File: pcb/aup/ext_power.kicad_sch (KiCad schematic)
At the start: 12 parts, among them J1 USB_C_Receptacle_USB2.0_16P, J2 Barral_Jack_12V, Q1 AO3401A, Q2 AO3401A, U2 USBLC6-2SC6

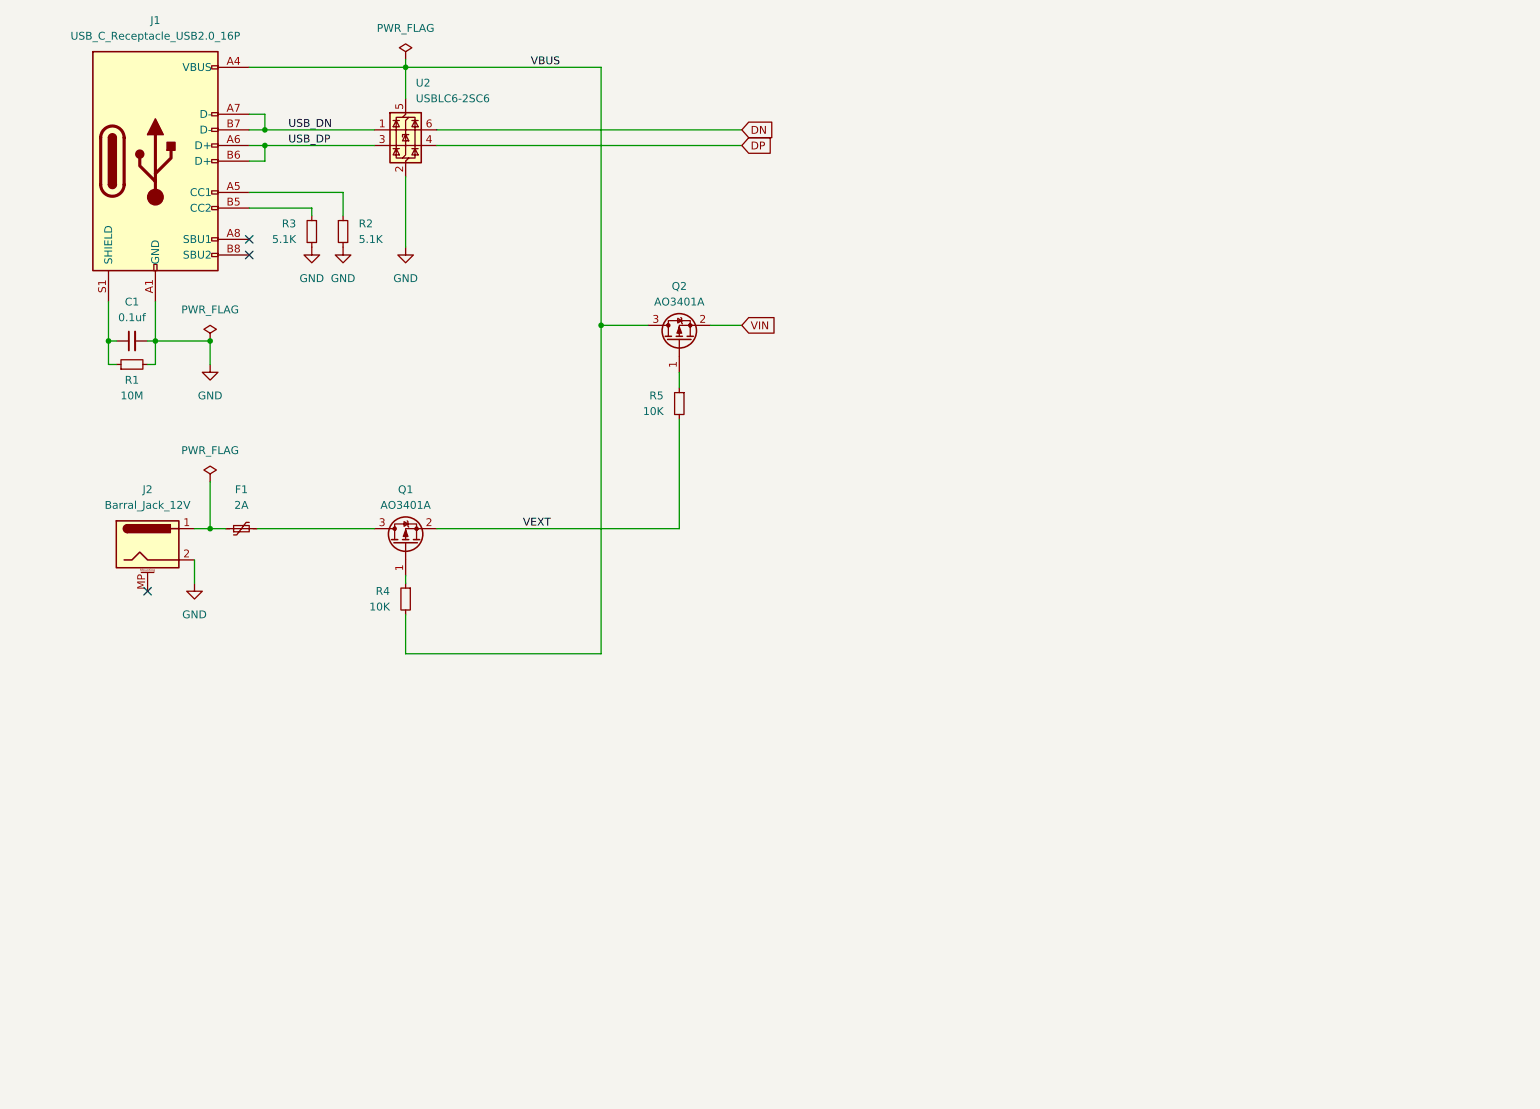
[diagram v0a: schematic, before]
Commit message: Add 5v regulator to external power portion
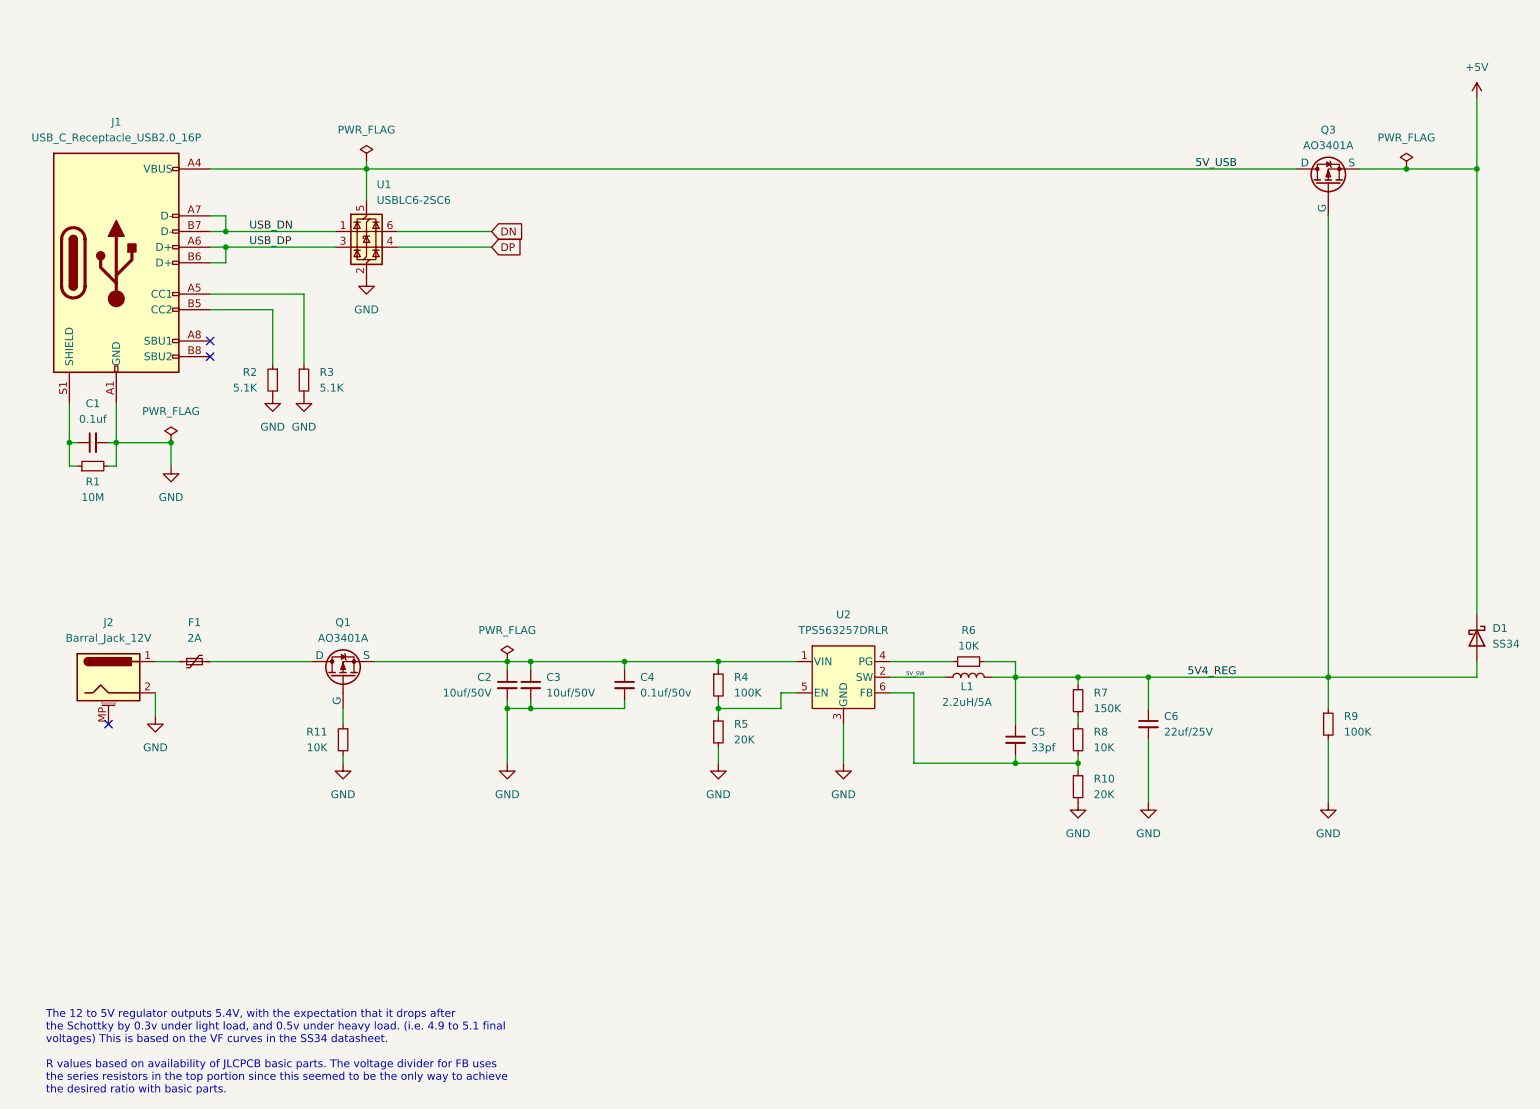
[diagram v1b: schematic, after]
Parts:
- removed R4, R5: 10K, Resistor_SMD:R_0603_1608Metric, symbol !Misc:R_10K_0603
- added C2, C3: 10uf/50V, Capacitor_SMD:C_0805_2012Metric, symbol !Misc:C_10uf_0805
- added C4: 0.1uf/50v, Capacitor_SMD:C_0603_1608Metric, symbol !Misc:C_0.1uf_0603
- added C5: 33pf, Capacitor_SMD:C_0402_1005Metric, symbol !Misc:C_33pf_0402
- added C6: 22uf/25V, Capacitor_SMD:C_0805_2012Metric, symbol !Misc:C_22uf_0805
- added D1: SS34, Diode_SMD:D_SMA, symbol !Misc:SS34
- added L1: 2.2uH/5A, Inductor_SMD:L_Sunlord_MWSA0518S, symbol !Misc:L_2.2uh_5A
- added R10, R5: 20K, Resistor_SMD:R_0603_1608Metric, symbol !Misc:R_20K_0603
- added R11, R6, R8: 10K, Resistor_SMD:R_0603_1608Metric, symbol !Misc:R_10K_0603
- added R4, R9: 100K, Resistor_SMD:R_0603_1608Metric, symbol !Misc:R_100K_0603
- added R7: 150K, Resistor_SMD:R_0603_1608Metric, symbol !Misc:R_150K_0603
- added U2: TPS563257DRLR, Package_TO_SOT_SMD:SOT-563, symbol !Misc:TPS563257DRLR
- renumbered Q2 to Q3, R3 to R2, R2 to R3, U2 to U1
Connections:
- net GND: now also C2.2, C3.2, C4.2, C6.2, R10.2, R11.2, R5.2, R9.2, U2.3 (GND)
- net at Q1.1 (G): now also R11.1
- net 5V4_REG: now reaches Q3.1 (G)
- net 5V4_REG: now also C5.1, C6.1, D1.2 (A), L1.2, R6.2, R7.1, R9.1
- net VBUS renamed 5V_USB
- net VEXT: no longer names the net of Q1.2 (S)
- net VEXT: now also C2.1, C3.1, C4.1, R4.1, U2.1 (VIN)
- net VIN renamed +5V
- net +5V: now also D1.1 (K)
- new net: R7.2, R8.1
- new net: R6.1, U2.4 (PG)
- new net: R4.2, R5.1, U2.5 (EN)
- new net: C5.2, R10.1, R8.2, U2.6 (FB)
- new net 5V_SW: L1.1, U2.2 (SW)
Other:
- note added: "The 12 to 5V regulator outputs 5.4V, with the expectation that it drops after the Schottky by 0.3v under light load, and 0.5v under heavy load. (i.e. 4.9 to 5.1 final voltages) This is based on the VF curves in the SS34 datasheet. R values based on availability of JLCPCB basic parts. The voltage divider for FB uses the series resistors in the top portion since this seemed to be the only way to ac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"
- moved on the sheet: C1, F1, J1, J2, Q3, R1, R2, R3, U1

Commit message: Start of fpga voltage rails. Added 1v0/vccint
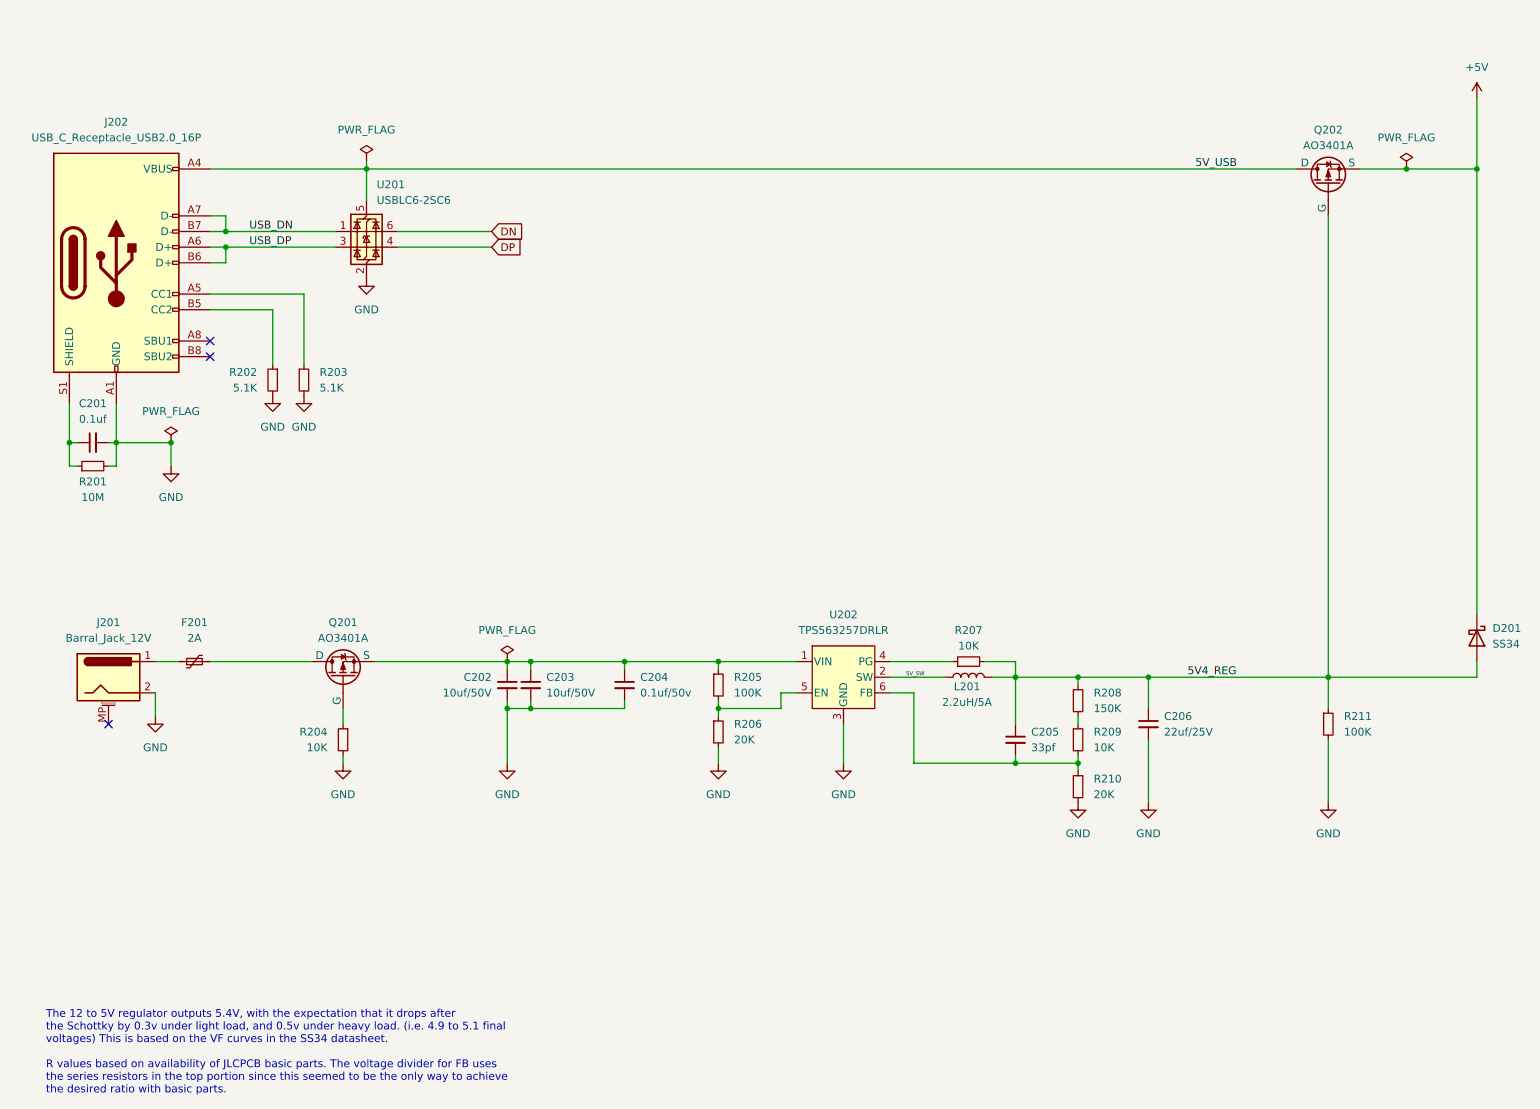
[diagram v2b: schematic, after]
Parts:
- renumbered C1 to C201, C2 to C202, C3 to C203, C4 to C204, C5 to C205, C6 to C206, D1 to D201, F1 to F201, J2 to J201, J1 to J202, L1 to L201, Q1 to Q201, Q3 to Q202, R1 to R201, R2 to R202, R3 to R203, R11 to R204, R4 to R205, R5 to R206, R6 to R207, R7 to R208, R8 to R209, R10 to R210, R9 to R211, U1 to U201, U2 to U202

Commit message: Finished voltage rail schematic
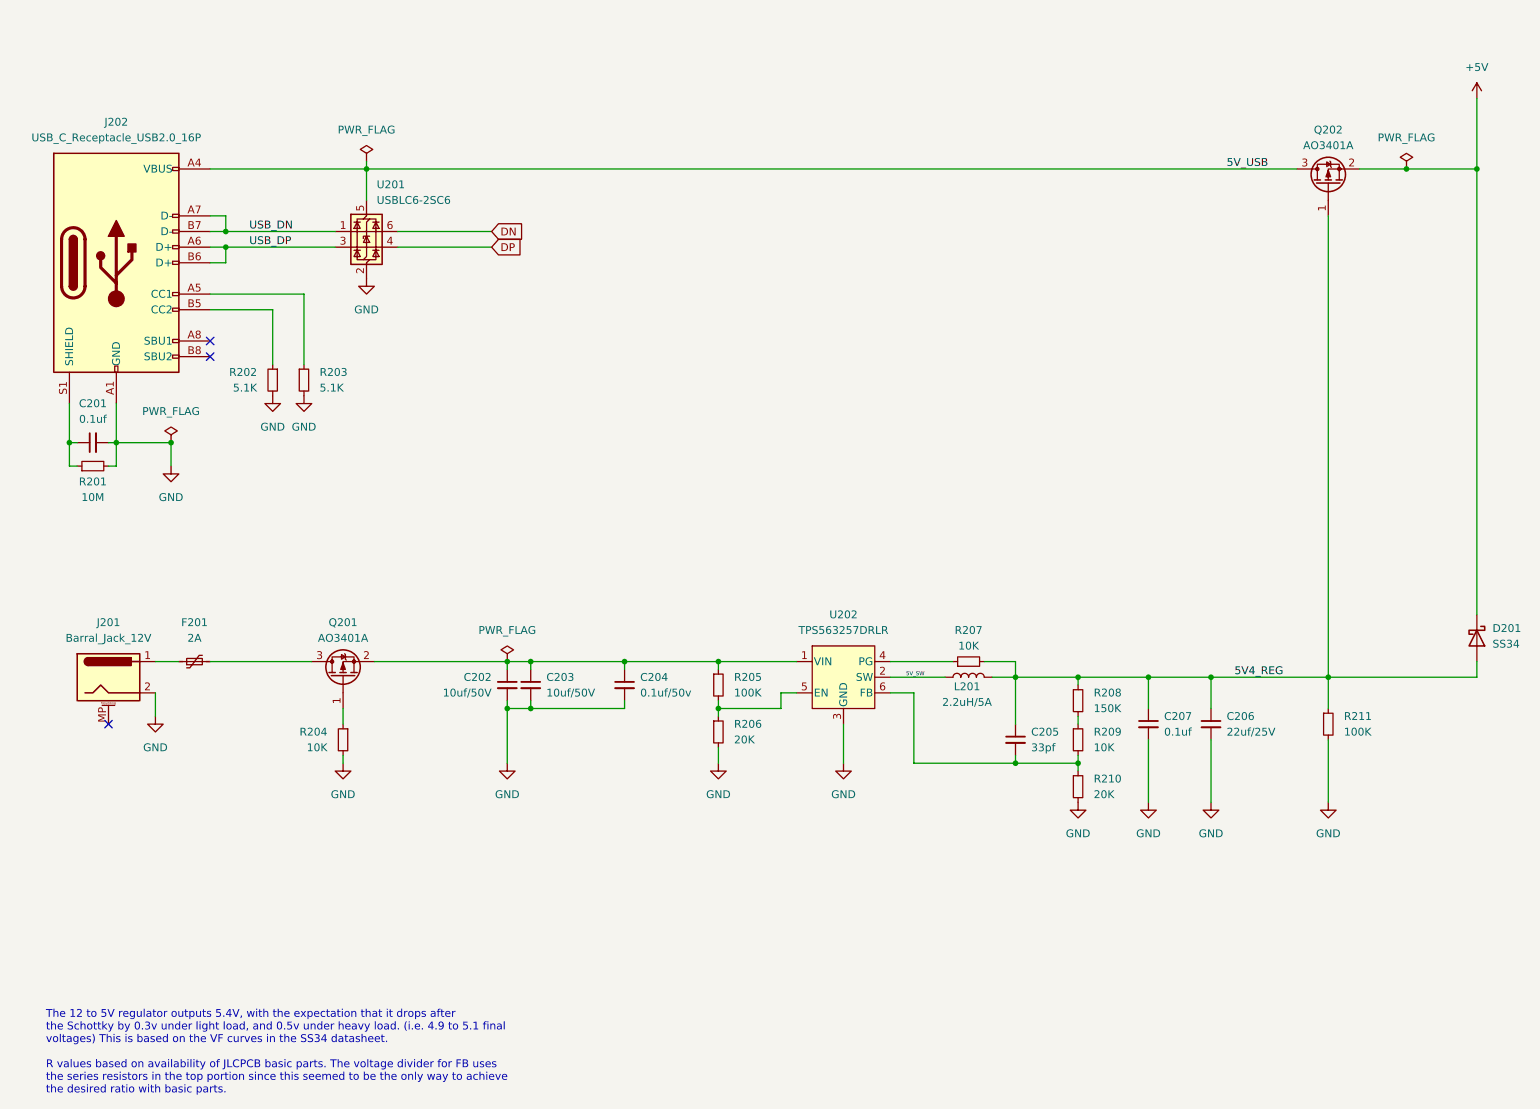
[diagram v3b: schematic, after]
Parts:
- added C207: 0.1uf, Capacitor_SMD:C_0402_1005Metric, symbol !Misc:C_0.1uf_0402
- U202: footprint Package_TO_SOT_SMD:SOT-563 -> SOT6_DRL_TEX
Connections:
- net 5V4_REG: now also C207.1
- net GND: now also C207.2
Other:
- moved on the sheet: C206
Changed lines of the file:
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@@
 	)
 	(junction
+		(at 209.55 128.27)
+		(diameter 0)
+		(color 0 0 0 0)
+	)
+	(junction
 		(at 72.39 45.72)
 		(diameter 0)
@@
 	(wire
 		(pts
+			(xy 209.55 138.43) (xy 209.55 148.59)
+		)
+		(stroke
+			(width 0)
+			(type default)
+		)
+	)
+	(wire
+		(pts
 			(xy 38.1 130.81) (xy 38.1 134.62)
 		)
@@
 	(wire
 		(pts
+			(xy 209.55 128.27) (xy 228.6 128.27)
+		)
+		(stroke
+			(width 0)
+			(type default)
+		)
+	)
+	(wire
+		(pts
 			(xy 252.73 125.73) (xy 252.73 128.27)
 		)
@@
 	(wire
 		(pts
+			(xy 209.55 128.27) (xy 209.55 133.35)
+		)
+		(stroke
+			(width 0)
+			(type default)
+		)
+	)
+	(wire
+		(pts
 			(xy 187.96 134.62) (xy 187.96 135.89)
 		)
@@
 	(wire
 		(pts
-			(xy 199.39 128.27) (xy 228.6 128.27)
+			(xy 199.39 128.27) (xy 209.55 128.27)
 		)
 		(stroke
@@
 	)
 	(label "5V_USB"
-		(at 207.01 45.72 0)
+		(at 212.09 45.72 0)
 		(effects
 			(font
@@
 	)
 	(label "5V4_REG"
-		(at 205.74 128.27 0)
+		(at 213.36 128.27 0)
 		(effects
 			(font
@@
 			)
 		)
-		(property "Footprint" "Package_TO_SOT_SMD:SOT-563"
+		(property "Footprint" "SOT6_DRL_TEX"
 			(at 136.906 116.586 0)
 			(effects
@@
 	)
 	(symbol
+		(lib_id "power:GND")
+		(at 209.55 148.59 0)
+		(unit 1)
+		(exclude_from_sim no)
+		(in_bom yes)
+		(on_board yes)
+		(dnp no)
+		(fields_autoplaced yes)
+		(property "Reference" "#PWR0216"
+			(at 209.55 154.94 0)
+			(effects
+				(font
+					(size 1.27 1.27)
+				)
+				(hide yes)
+			)
+		)
+		(property "Value" "GND"
+			(at 209.55 153.67 0)
+			(effects
+				(font
+					(size 1.27 1.27)
+				)
+			)
+		)
+		(property "Footprint" ""
+			(at 209.55 148.59 0)
+			(effects
+				(font
+					(size 1.27 1.27)
+				)
+				(hide yes)
+			)
+		)
+		(property "Datasheet" ""
+			(at 209.55 148.59 0)
+			(effects
+				(font
+					(size 1.27 1.27)
+				)
+				(hide yes)
+			)
+		)
+		(property "Description" "Power symbol creates a global label with name \"GND\" , ground"
+			(at 209.55 148.59 0)
+			(effects
+				(font
+					(size 1.27 1.27)
+				)
+				(hide yes)
+			)
+		)
+		(pin "1"
+		)
+		(instances
+			(project "aup"
+				(path "/312a869c-f247-4883-8e23-bdad51e1754f/66f6f111-4301-4b77-9bf5-52f6219d7e81"
+					(reference "#PWR0216")
+					(unit 1)
+				)
+			)
+		)
+	)
+	(symbol
 		(lib_id "!Misc:USBLC6-2SC6")
 		(at 72.39 55.88 0)
@@
 	)
 	(symbol
-		(lib_name "AO3401A_1")
 		(lib_id "!Misc:AO3401A")
 		(at 68.58 128.27 90)
@@
 	)
 	(symbol
+		(lib_id "!Misc:C_0.1uf_0402")
+		(at 199.39 135.89 0)
+		(unit 1)
+		(exclude_from_sim no)
+		(in_bom yes)
+		(on_board yes)
+		(dnp no)
+		(fields_autoplaced yes)
+		(property "Reference" "C207"
+			(at 201.93 134.6262 0)
+			(effects
+				(font
+					(size 1.27 1.27)
+				)
+				(justify left)
+			)
+		)
+		(property "Value" "0.1uf"
+			(at 201.93 137.1662 0)
+			(effects
+				(font
+					(size 1.27 1.27)
+				)
+				(justify left)
+			)
+		)
+		(property "Footprint" "Capacitor_SMD:C_0402_1005Metric"
+			(at 199.39 135.89 0)
+			(effects
+				(font
+					(size 1.27 1.27)
+				)
+				(hide yes)
+			)
+		)
+		(property "Datasheet" "~"
+			(at 199.39 135.89 0)
+			(effects
+				(font
+					(size 1.27 1.27)
+				)
+				(hide yes)
+			)
+		)
+		(property "Description" "Unpolarized capacitor 0.1uf 0402"
+			(at 199.39 135.89 0)
+			(effects
+				(font
+					(size 1.27 1.27)
+				)
+				(hide yes)
+			)
+		)
+		(property "LCSC Part #" "C1525"
+			(at 199.39 135.89 0)
+			(effects
+				(font
+					(size 1.27 1.27)
+				)
+				(hide yes)
+			)
+		)
+		(property "Digi-Key Part Number" "490-6328-1-ND"
+			(at 199.39 135.89 0)
+			(effects
+				(font
+					(size 1.27 1.27)
+				)
+				(hide yes)
+			)
+		)
+		(pin "2"
+		)
+		(pin "1"
+		)
+		(instances
+			(project ""
+				(path "/312a869c-f247-4883-8e23-bdad51e1754f/66f6f111-4301-4b77-9bf5-52f6219d7e81"
+					(reference "C207")
+					(unit 1)
+				)
+			)
+		)
+	)
+	(symbol
 		(lib_id "!Misc:R_10K_0603")
 		(at 68.58 138.43 0)
@@
 	(symbol
 		(lib_id "!Misc:C_22uf_0805")
-		(at 199.39 135.89 0)
+		(at 209.55 135.89 0)
 		(unit 1)
 		(exclude_from_sim no)
@@
 		(fields_autoplaced yes)
 		(property "Reference" "C206"
-			(at 201.93 134.6262 0)
+			(at 212.09 134.6262 0)
 			(effects
 				(font
@@
 		)
 		(property "Value" "22uf/25V"
-			(at 201.93 137.1662 0)
+			(at 212.09 137.1662 0)
 			(effects
 				(font
@@
 		)
 		(property "Footprint" "Capacitor_SMD:C_0805_2012Metric"
-			(at 199.39 135.89 0)
+			(at 209.55 135.89 0)
 			(effects
 				(font
@@
 		)
 		(property "Datasheet" "~"
-			(at 199.39 135.89 0)
+			(at 209.55 135.89 0)
 			(effects
 				(font
@@
 		)
 		(property "Description" "Unpolarized capacitor 22uf 0805 25V"
-			(at 199.39 135.89 0)
+			(at 209.55 135.89 0)
 			(effects
 				(font
@@
 		)
 		(property "LCSC Part #" "C45783"
-			(at 199.39 135.89 0)
+			(at 209.55 135.89 0)
 			(effects
 				(font
@@
 		)
 		(property "Digi-Key Part Number" "490-14661-1-ND"
-			(at 199.39 135.89 0)
+			(at 209.55 135.89 0)
 			(effects
 				(font
